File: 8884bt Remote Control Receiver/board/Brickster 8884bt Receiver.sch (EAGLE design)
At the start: 23 parts, among them J1 AVR_SPI_PRG_6NS, U2 TB6621FNG

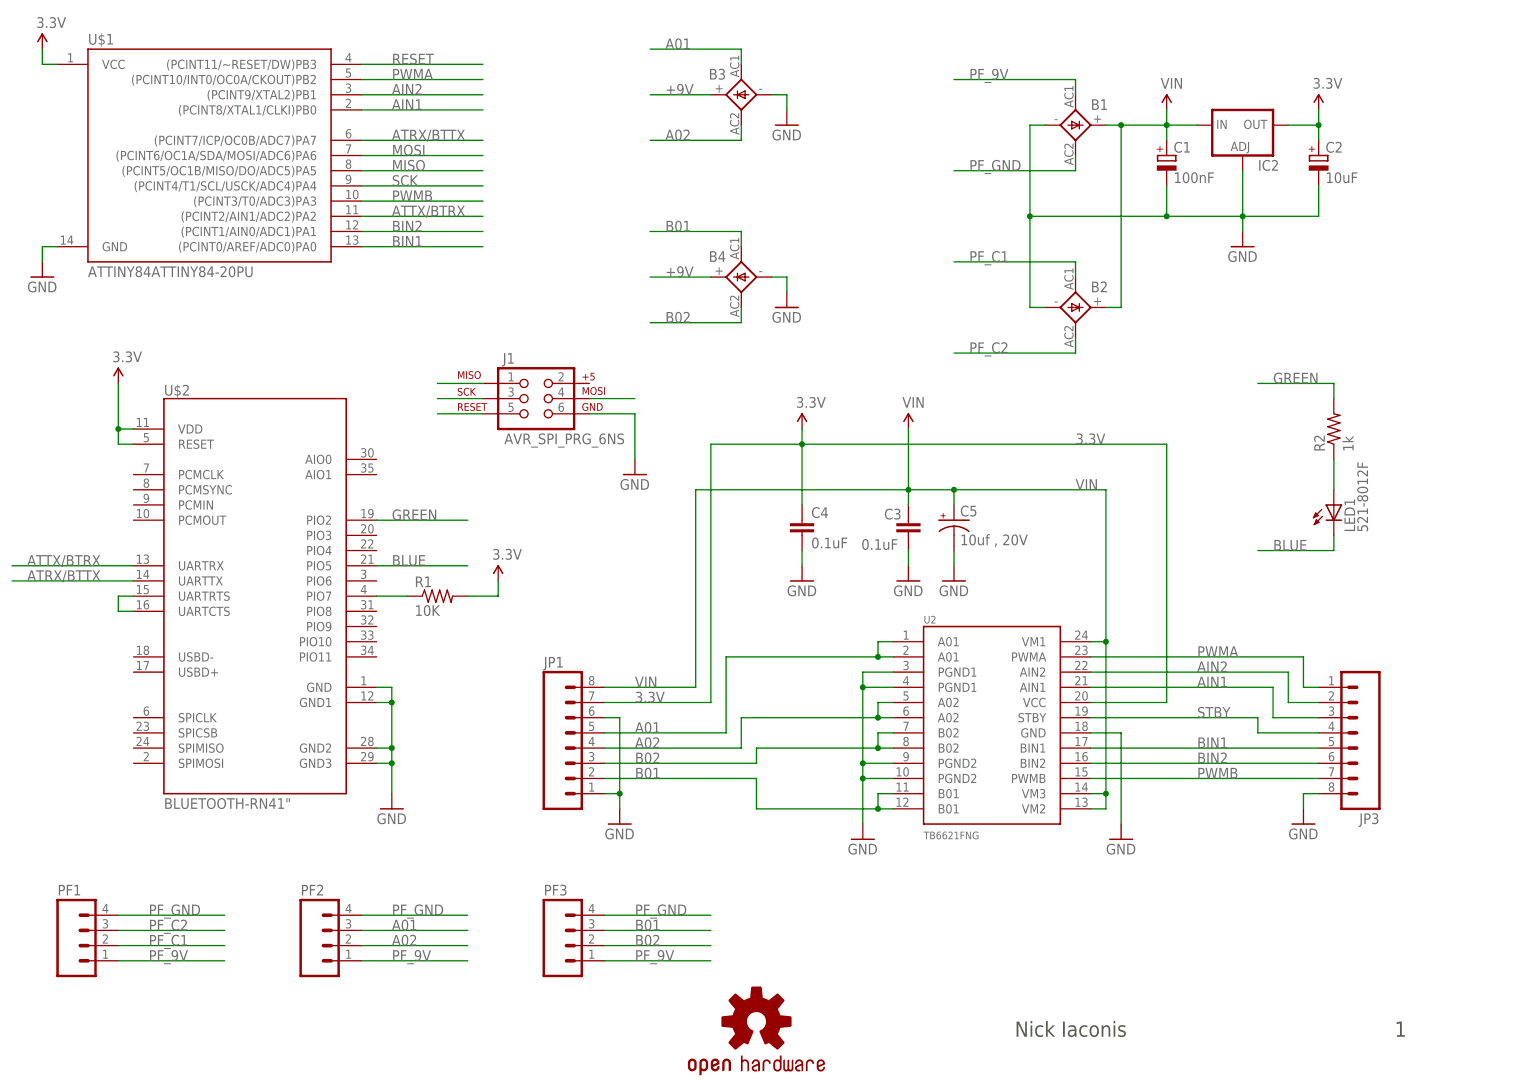
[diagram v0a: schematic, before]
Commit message: Update schematic components +New components include device footprints
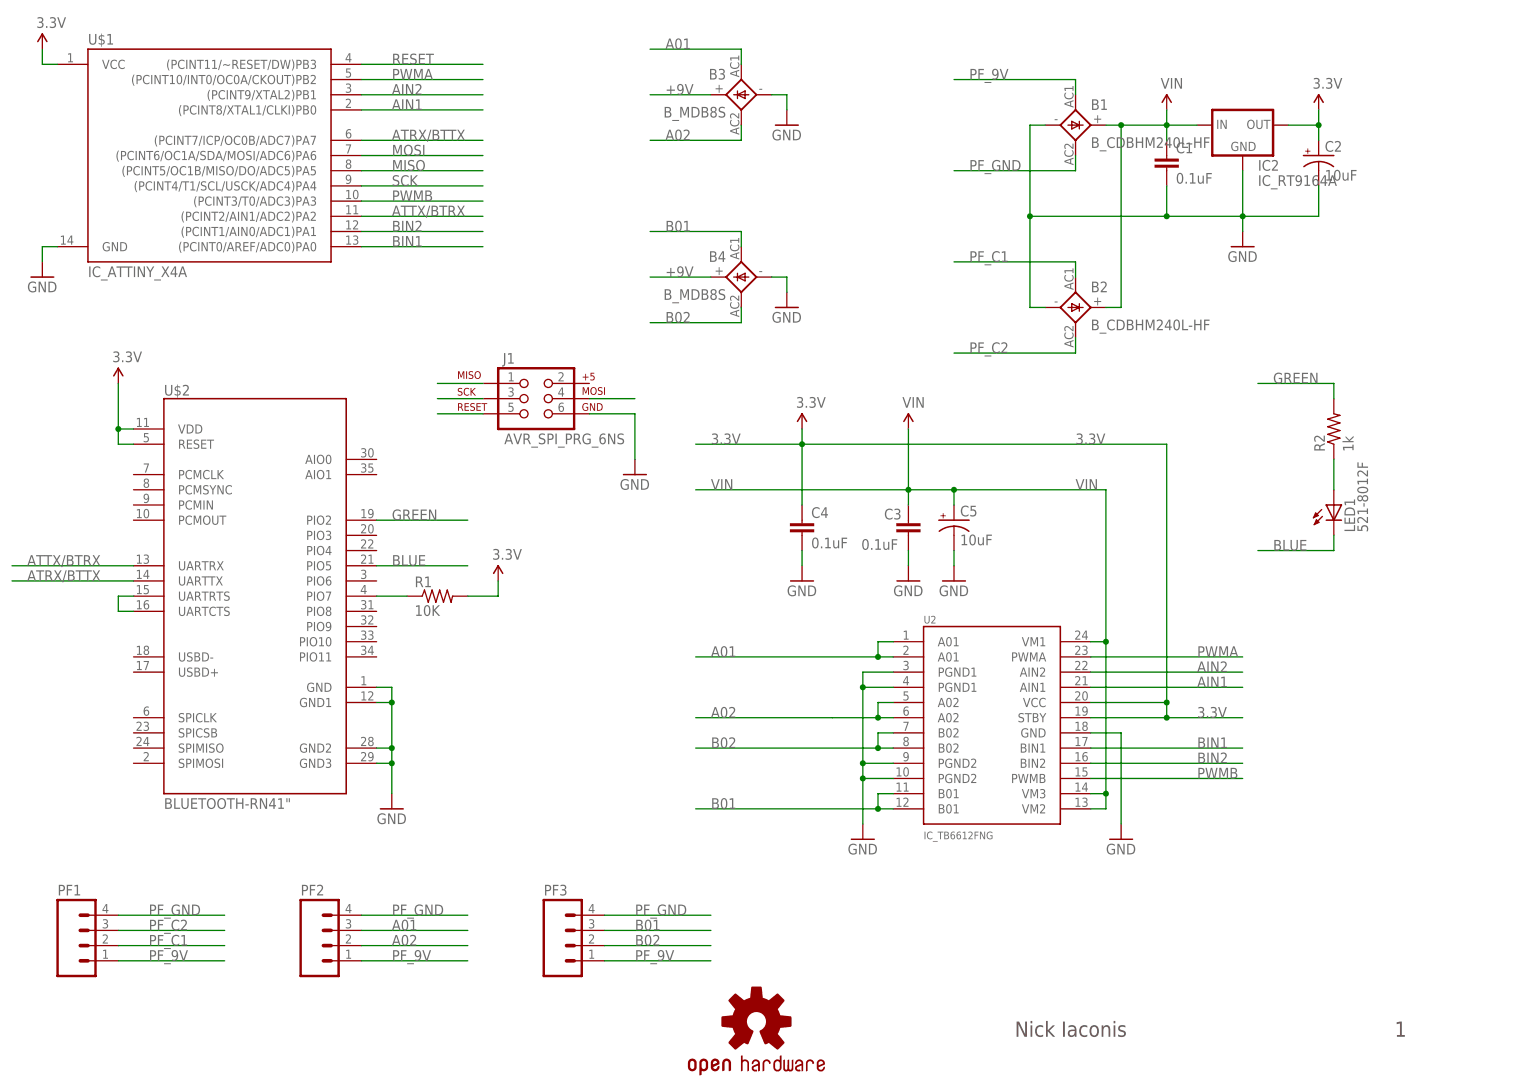
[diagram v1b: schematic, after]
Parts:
- removed JP1, JP3: (no value), SparkFun:M08LONGPADS
- B1, B2: value (none) -> B_CDBHM240L-HF; device rectifier:2KBB-R -> brickster:B_CDBHM240L-HF
- B3, B4: value (none) -> B_MDB8S; device rectifier:2KBB-R -> brickster:B_MDB8S
- C1: value 100nF -> 0.1uF; device rcl:CPOL-EUE10-20 -> brickster:C
- C2: device rcl:CPOL-EUE10-20 -> brickster:C_POL
- C3, C4: device SparkFun:CAP0402-CAP -> brickster:C
- C5: value 10uf , 20V -> 10uF; device SparkFun:CAP_POL3528 -> brickster:C_POL
- IC2: value (none) -> IC_RT9164A; device v-reg:LM317TS -> brickster:IC_RT9164A
- R1: device SparkFun-Resistors:10KOHM1/10W1%(0603)0603 -> brickster:R
- R2: device SparkFun-Resistors:RESISTOR0805-RES -> brickster:R
- U$1: value ATTINY84ATTINY84-20PU -> IC_ATTINY_X4A; device SparkFun-DigitalIC:ATTINY84ATTINY84-20PU -> brickster:IC_ATTINY_X4A
- U2: value TB6621FNG -> IC_TB6612FNG; device SparkFun:TB6621FNG -> brickster:IC_TB6612FNG
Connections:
- removed net STBY: JP3.4, U2.STBY
- net 3.3V: now also U2.STBY; no longer JP1.7
- net A01: no longer JP1.5
- net A02: no longer JP1.4
- net AIN1: no longer JP3.3
- net AIN2: no longer JP3.2
- net B01: no longer JP1.2
- net B02: no longer JP1.3
- net BIN1: no longer JP3.5
- net BIN2: no longer JP3.6
- net GND: now also C1.2, IC2.GND; no longer C1.-, IC2.ADJ, JP1.1, JP1.6, JP3.8
- net PWMA: no longer JP3.1
- net PWMB: no longer JP3.7
- net VIN: now also C1.1; no longer C1.+, JP1.8

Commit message: Include parts library with source
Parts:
- removed LED1: 521-8012F, led:LED3MM
- added D1: LED_LTST_C195TBKFKT, brickster:LED_LTST_C195TBKFKT
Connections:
- net BLUE: no longer LED1.C
- net N$16: no longer LED1.A
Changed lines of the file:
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@@
 <part name="U$1" library="brickster" deviceset="IC_ATTINY_X4A" device=""/>
 <part name="R2" library="brickster" deviceset="R" device="" value="1k"/>
-<part name="LED1" library="led" deviceset="LED" device="3MM" value="521-8012F"/>
 <part name="U2" library="brickster" deviceset="IC_TB6612FNG" device=""/>
 <part name="C3" library="brickster" deviceset="C" device="" value="0.1uF"/>
@@
 <part name="C2" library="brickster" deviceset="C_POL" device="" value="10uF"/>
 <part name="C5" library="brickster" deviceset="C_POL" device="" value="10uF"/>
+<part name="D1" library="brickster" deviceset="LED_LTST_C195TBKFKT" device=""/>
 </parts>
 <sheets>
@@
 <instance part="U$1" gate="G$1" x="144.78" y="175.26"/>
 <instance part="R2" gate="G$1" x="332.74" y="129.54" rot="R90"/>
-<instance part="LED1" gate="G$1" x="332.74" y="116.84"/>
 <instance part="U2" gate="G$1" x="276.86" y="81.28"/>
 <instance part="C3" gate="G$1" x="261.62" y="111.76" smashed="yes">
@@
 <instance part="C2" gate="G$1" x="330.2" y="175.26"/>
 <instance part="C5" gate="G$1" x="269.24" y="114.3"/>
+<instance part="D1" gate="G$1" x="340.36" y="116.84"/>
+<instance part="D1" gate="G$2" x="340.36" y="104.14"/>
 </instances>
 <busses>
@@
 <net name="N$16" class="0">
 <segment>
-<pinref part="LED1" gate="G$1" pin="A"/>
 <pinref part="R2" gate="G$1" pin="1"/>
 <wire x1="332.74" y1="124.46" x2="332.74" y2="119.38" width="0.1524" layer="91"/>
@@
 <net name="BLUE" class="0">
 <segment>
-<pinref part="LED1" gate="G$1" pin="C"/>
 <wire x1="332.74" y1="111.76" x2="332.74" y2="109.22" width="0.1524" layer="91"/>
 <wire x1="332.74" y1="109.22" x2="320.04" y2="109.22" width="0.1524" layer="91"/>

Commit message: Prepare repository for board layout
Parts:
- added D2: D, brickster:D
- D1: value LED_LTST_C195TBKFKT -> Blue/Orange
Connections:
- net GREEN renamed ORANGE
- removed net +9V: B3.+, B4.+
- removed net PF_GND: B1.AC2, PF1.4, PF2.4, PF3.4
- new net N$1: D2.P$1, J1.2
- net BLUE: now also D1G$1.P$1, D1G$2.P$2
- net GND: now also B1.AC2, PF1.4, PF2.4, PF3.4
- net N$16: now also D1G$1.P$2, D1G$2.P$1
- net VIN: now also B3.+, B4.+, D2.P$2
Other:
- moved on the sheet: D1G$1, D1G$2, PF1, PF2, PF3

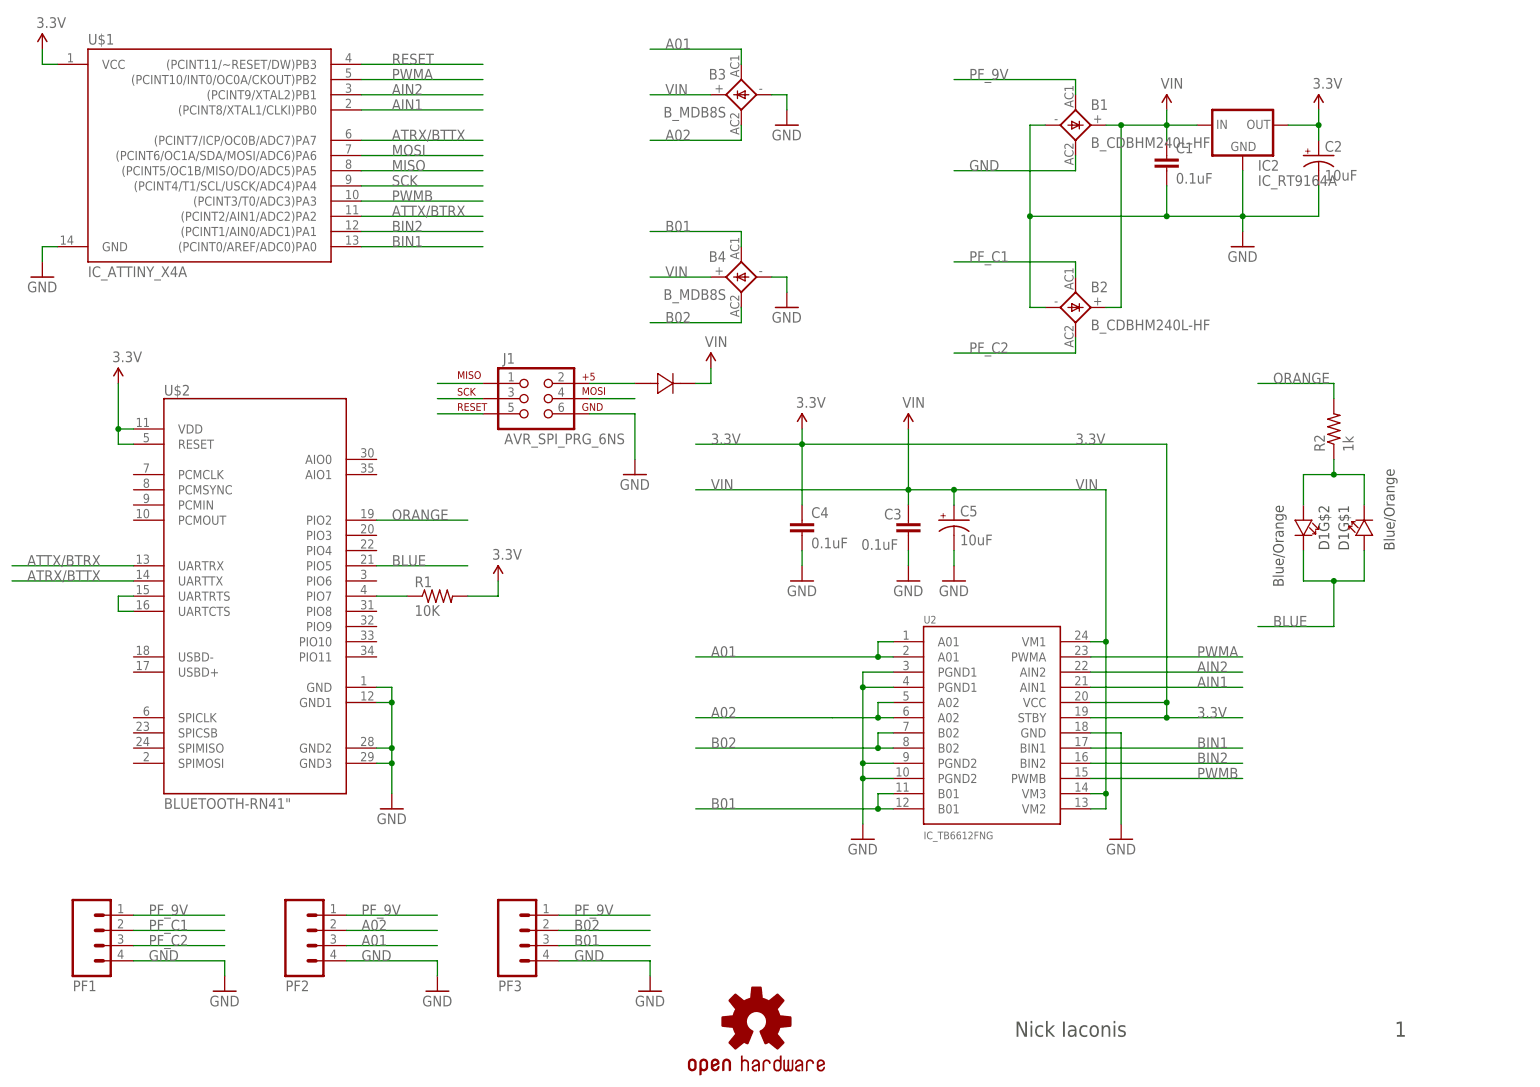
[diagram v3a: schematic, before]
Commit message: Layout PCB
+Revision 1 (uses RN-41/42)
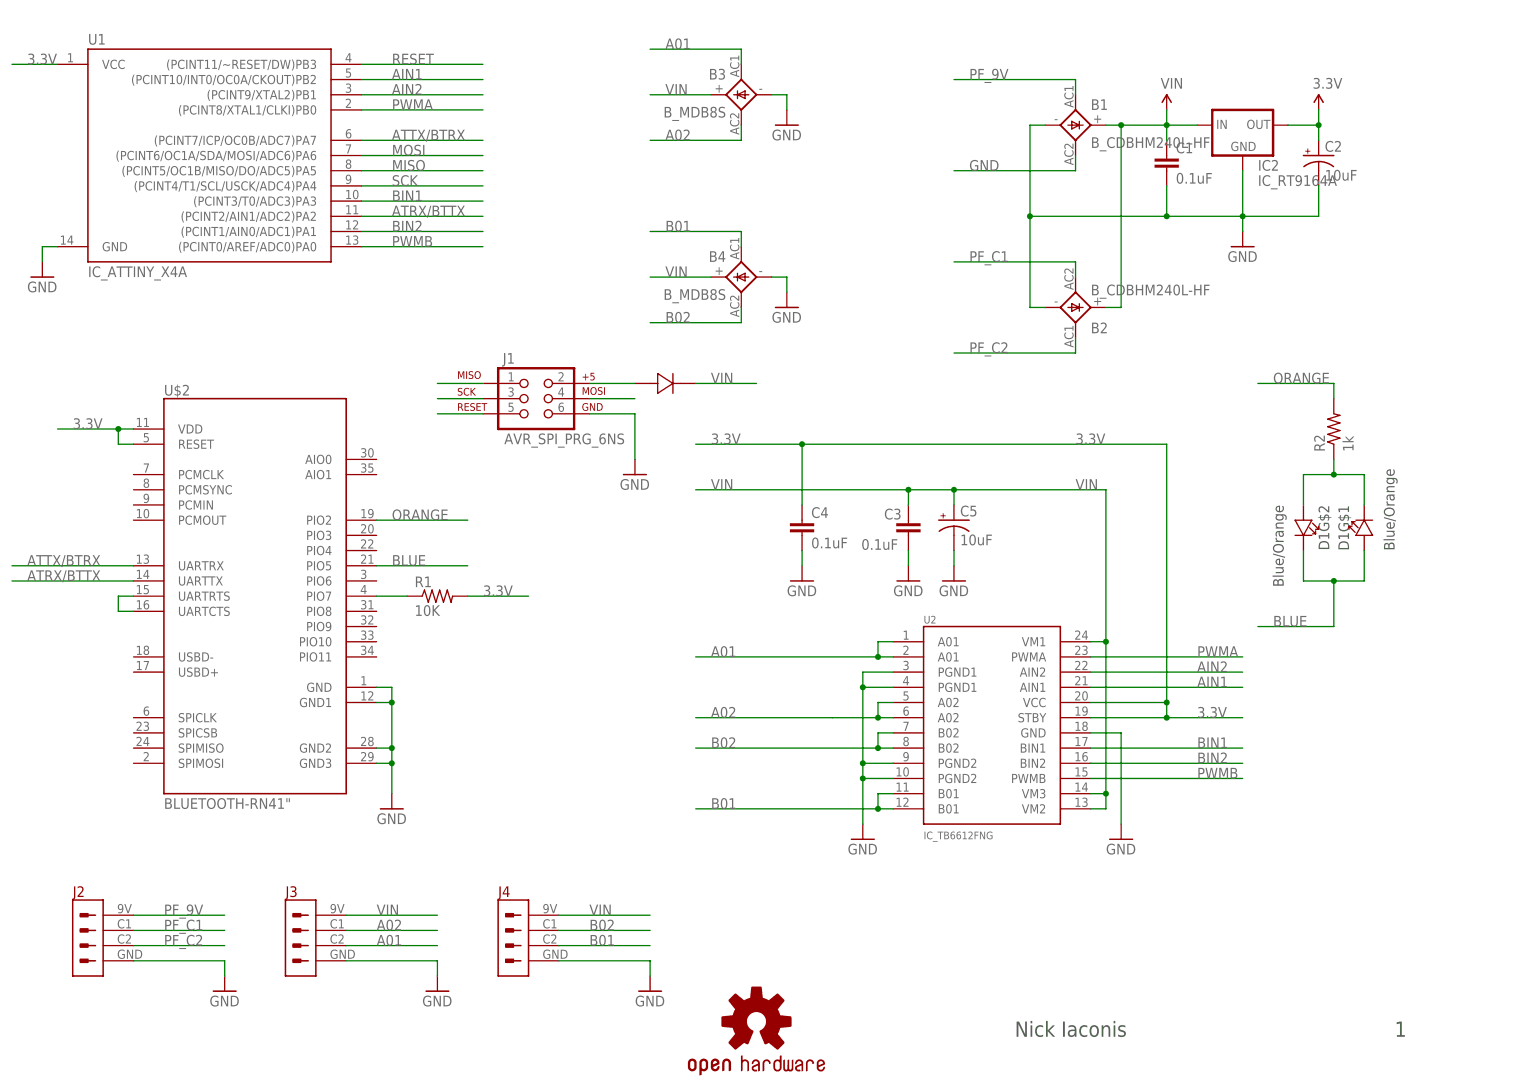
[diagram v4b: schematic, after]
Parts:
- removed PF1, PF2, PF3: (no value), SparkFun-Connectors:M04PTH
- added J2, J3, J4: CON_PF, brickster:CON_PF
- renumbered U$1 to U1
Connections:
- net A01: now also J3.P$3; no longer PF2.3
- net A02: now also J3.P$2; no longer PF2.2
- net AIN1: now also U1.(PCINT10/INT0/OC0A/CKOUT)PB2; no longer U1.(PCINT8/XTAL1/CLKI)PB0
- net ATRX/BTTX: now also U1.(PCINT2/AIN1/ADC2)PA2; no longer U1.(PCINT7/ICP/OC0B/ADC7)PA7
- net ATTX/BTRX: now also U1.(PCINT7/ICP/OC0B/ADC7)PA7; no longer U1.(PCINT2/AIN1/ADC2)PA2
- net B01: now also J4.P$3; no longer PF3.3
- net B02: now also J4.P$2; no longer PF3.2
- net BIN1: now also U1.(PCINT3/T0/ADC3)PA3; no longer U1.(PCINT0/AREF/ADC0)PA0
- net GND: now also J2.P$4, J3.P$4, J4.P$4; no longer PF1.4, PF2.4, PF3.4
- net PF_9V: now also J2.P$1; no longer PF1.1, PF2.1, PF3.1
- net PF_C1: now also B2.AC2, J2.P$2; no longer B2.AC1, PF1.2
- net PF_C2: now also B2.AC1, J2.P$3; no longer B2.AC2, PF1.3
- net PWMA: now also U1.(PCINT8/XTAL1/CLKI)PB0; no longer U1.(PCINT10/INT0/OC0A/CKOUT)PB2
- net PWMB: now also U1.(PCINT0/AREF/ADC0)PA0; no longer U1.(PCINT3/T0/ADC3)PA3
- net VIN: now also J3.P$1, J4.P$1
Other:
- moved on the sheet: B2
